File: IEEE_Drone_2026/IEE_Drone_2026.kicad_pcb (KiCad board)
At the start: 2 copper layers, 40.5 x 58 mm, 30 parts, among them IC1 TPSM84209RKHT, IC2 TPSM84209RKHT, J1 ESC, J10 M2, J11 Conn_01x02_Socket, J2 M4 Mounting, J3 M4 Mounting, J4 M4 Mounting, J5 M4 Mounting, J6 Pixy2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

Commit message: made production
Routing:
- net GND: vias 25 -> 27
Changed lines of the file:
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@@
+	)
+	(via
+		(at 99.06 65.532)
+		(size 0.6)
+		(drill 0.3)
+		(layers "F.Cu" "B.Cu")
+		(free yes)
+		(net 29)
+	)
+	(via
+		(at 99.06 64.643)
+		(size 0.6)
+		(drill 0.3)
+		(layers "F.Cu" "B.Cu")
+		(free yes)
+		(net 29)
 	)
 	(via

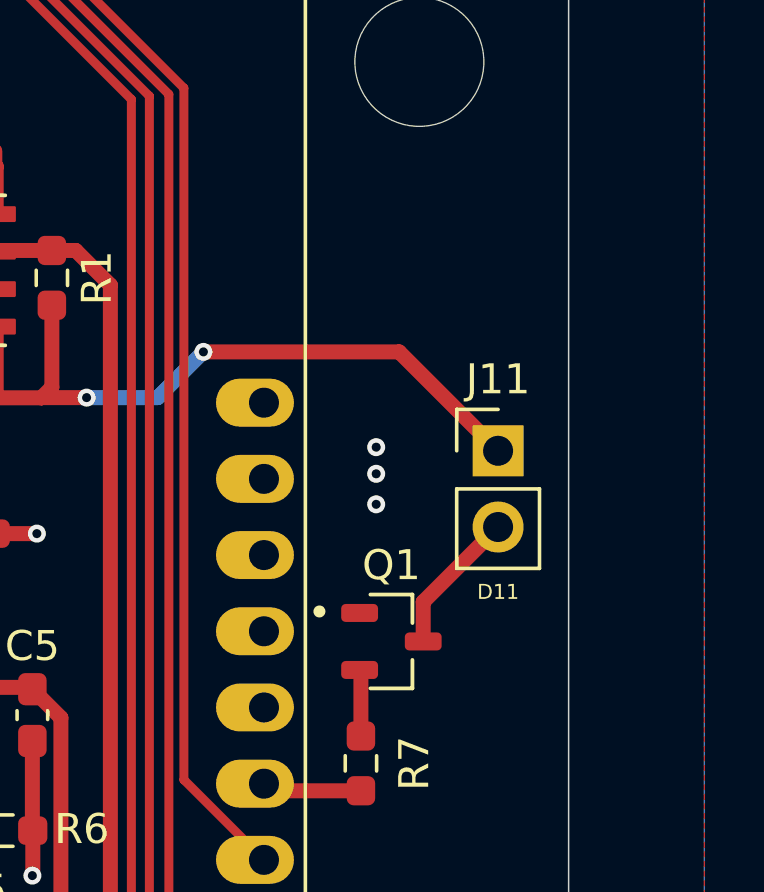
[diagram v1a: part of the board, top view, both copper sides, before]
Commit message: updated silkscreen text
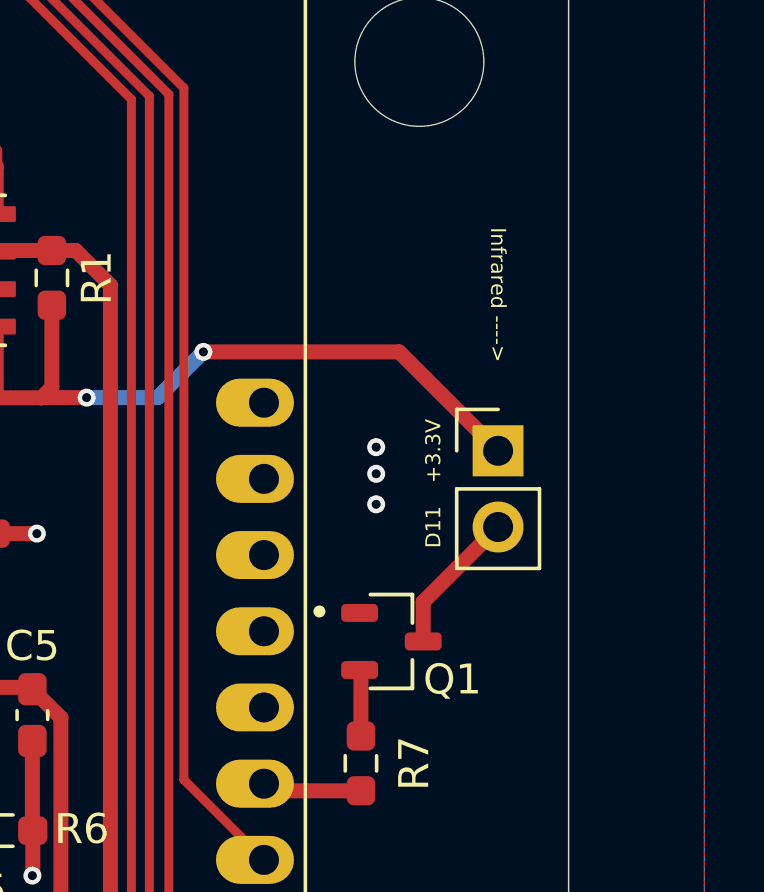
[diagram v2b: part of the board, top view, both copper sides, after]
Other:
- board text added: "Infrared ---->"
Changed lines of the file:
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@@
 			(at 0 -2.38 0)
 			(layer "F.SilkS")
+			(hide yes)
 			(effects
 				(font
@@
 		(at 99.568 71.12)
 		(property "Reference" "Q1"
-			(at 0 -2.54 0)
+			(at 2.032 1.27 0)
 			(layer "F.SilkS")
 			(effects
@@
 		)
 	)
+	(gr_text "Infrared ---->\n"
+		(at 103.124 59.563 270)
+		(layer "F.SilkS")
+		(effects
+			(font
+				(size 0.5 0.5)
+				(thickness 0.125)
+			)
+		)
+	)
 	(gr_text "SCK"
 		(at 69.6 63.8 90)
@@
 		)
 	)
+	(gr_text "+3.3V"
+		(at 100.965 64.77 90)
+		(layer "F.SilkS")
+		(effects
+			(font
+				(size 0.5 0.5)
+				(thickness 0.125)
+			)
+		)
+	)
 	(gr_text "D9\n"
 		(at 86 43.9 0)
@@
 	)
 	(gr_text "D11\n"
-		(at 103.124 69.469 0)
+		(at 100.965 67.31 90)
 		(layer "F.SilkS")
 		(effects

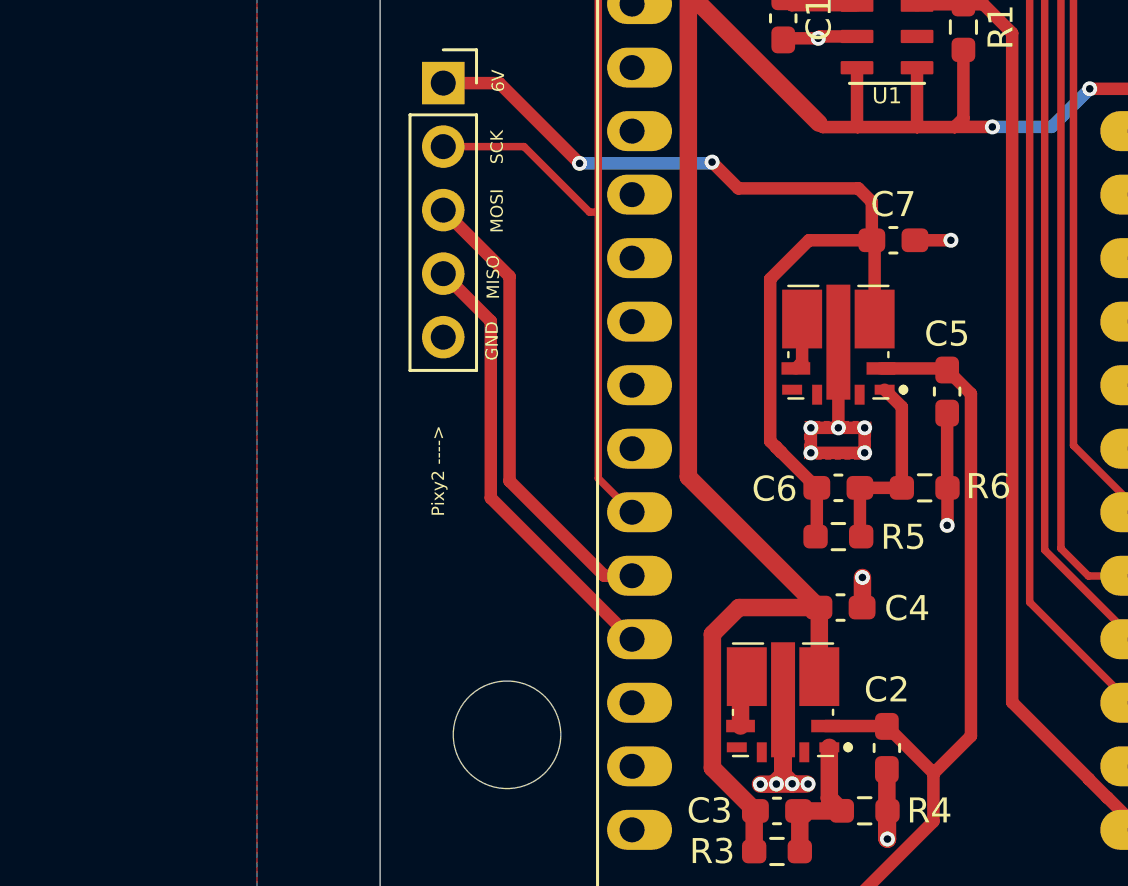
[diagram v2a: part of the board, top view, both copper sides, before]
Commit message: updated c4 c5 c7 to 1206
coudn't find 0603 in spec
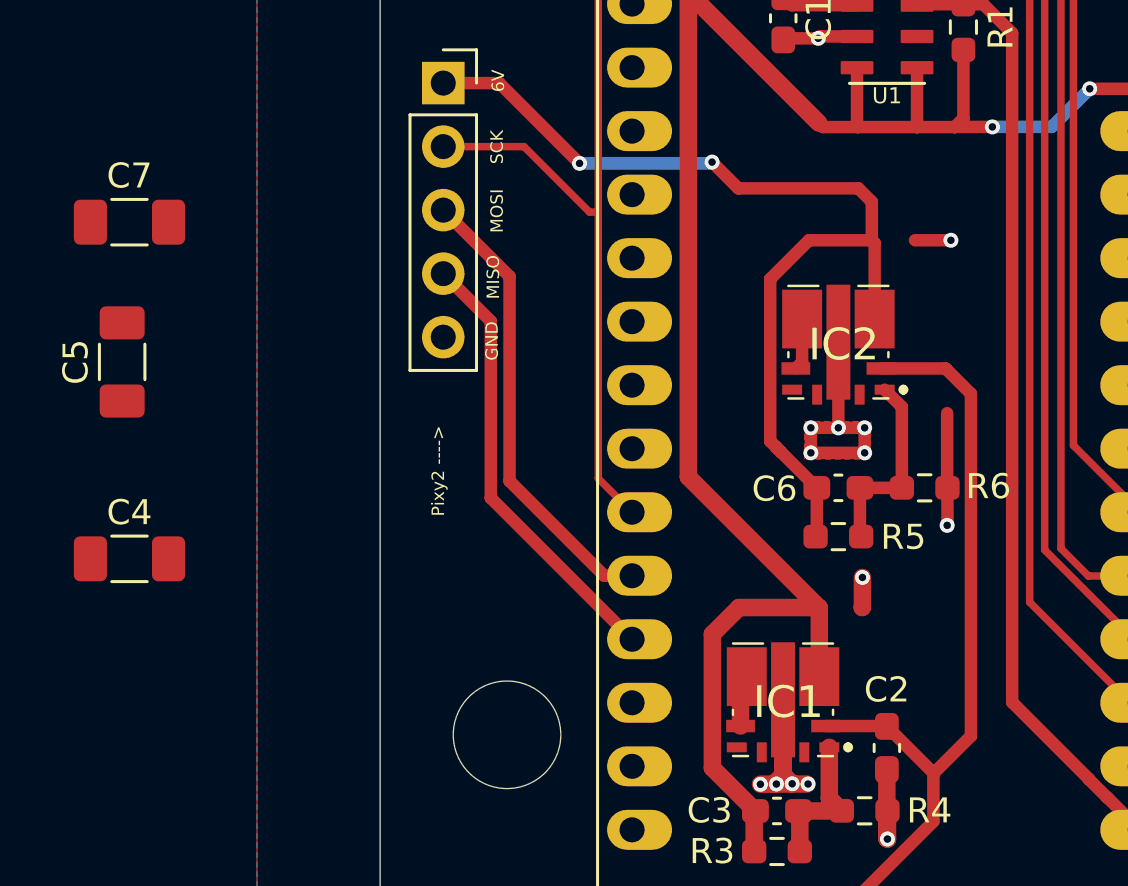
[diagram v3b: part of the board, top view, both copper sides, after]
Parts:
- C4, C5, C7: footprint Capacitor_SMD:C_0603_1608Metric_Pad1.08x0.95mm_HandSolder -> Capacitor_SMD:C_1206_3216Metric_Pad1.33x1.80mm_HandSolder
- R3, R5: value 10kOhm -> 10k
- R4: value 2.2kOhm -> 2.2k
- moved C5 33.0 mm to (54.6, 72.4)
- moved C7 30.6 mm to (54.9, 66.8)
- moved C4 28.5 mm to (54.9, 80.3)

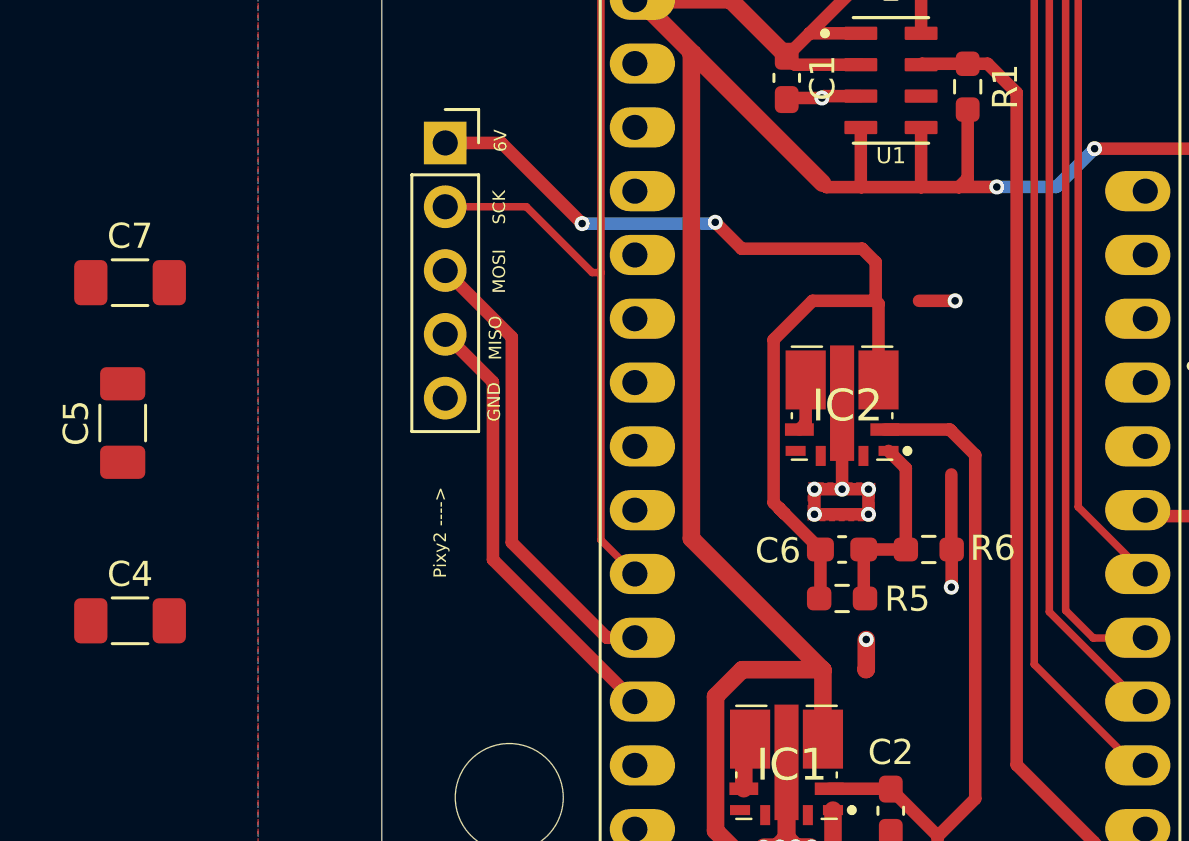
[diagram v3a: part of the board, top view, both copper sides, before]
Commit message: updated routing for 1206 caps
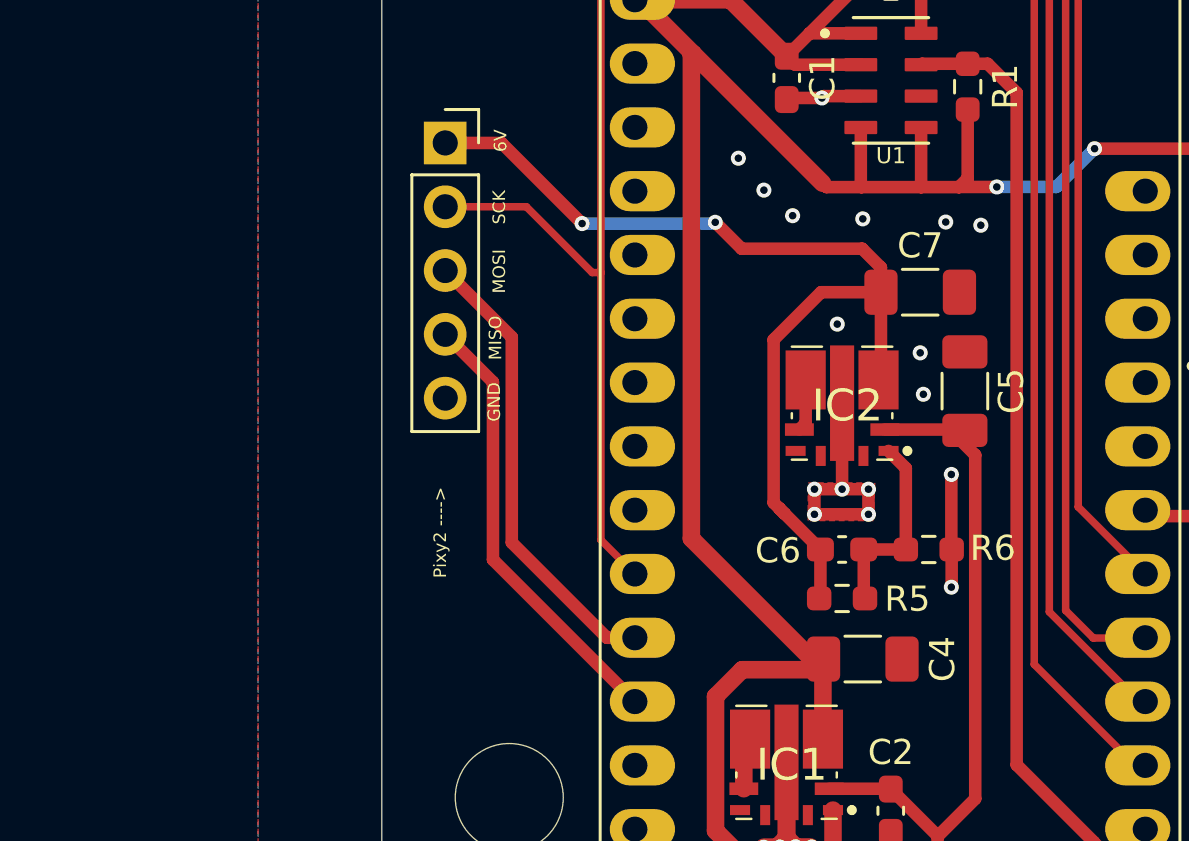
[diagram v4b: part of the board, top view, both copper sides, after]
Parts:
- moved C5 33.6 mm to (88.1, 71.1), turned to -90 degrees
- moved C7 31.5 mm to (86.4, 67.2)
- moved C4 29.2 mm to (84.1, 81.8)
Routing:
- net GND: track 33.4 -> 30.7 mm, vias 27 -> 35
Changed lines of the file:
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@@
 	(footprint "Capacitor_SMD:C_1206_3216Metric_Pad1.33x1.80mm_HandSolder"
 		(layer "F.Cu")
-		(at 54.9025 80.264)
+		(at 84.074 81.788)
 		(descr "Capacitor SMD 1206 (3216 Metric), square (rectangular) end terminal, IPC-7351 nominal with elongated pad for handsoldering. (Body size source: IPC-SM-782 page 76, https://www.pcb-3d.com/wordpress/wp-content/uploads/ipc-sm-782a_amendment_1_and_2.pdf), generated with kicad-footprint-generator")
 		(tags "capacitor handsolder")
 		(property "Reference" "C4"
-			(at 0 -1.85 0)
+			(at 3.175 0 90)
 			(layer "F.SilkS")
 			(effects
@@
 			(at 0 1.85 0)
 			(layer "F.Fab")
+			(hide yes)
 			(effects
 				(font
@@
 	(footprint "Capacitor_SMD:C_1206_3216Metric_Pad1.33x1.80mm_HandSolder"
 		(layer "F.Cu")
-		(at 54.61 72.39 90)
+		(at 88.138 71.12 -90)
 		(descr "Capacitor SMD 1206 (3216 Metric), square (rectangular) end terminal, IPC-7351 nominal with elongated pad for handsoldering. (Body size source: IPC-SM-782 page 76, https://www.pcb-3d.com/wordpress/wp-content/uploads/ipc-sm-782a_amendment_1_and_2.pdf), generated with kicad-footprint-generator")
 		(tags "capacitor handsolder")
@@
 			(at 0 1.85 90)
 			(layer "F.Fab")
+			(hide yes)
 			(effects
 				(font
@@
 		(attr smd)
 		(fp_line
-			(start -0.711252 -0.91)
-			(end 0.711252 -0.91)
+			(start -0.711252 0.91)
+			(end 0.711252 0.91)
 			(stroke
 				(width 0.12)
@@
 		)
 		(fp_line
-			(start -0.711252 0.91)
-			(end 0.711252 0.91)
+			(start -0.711252 -0.91)
+			(end 0.711252 -0.91)
 			(stroke
 				(width 0.12)
@@
 		)
 		(fp_line
-			(start 2.48 -1.15)
-			(end 2.48 1.15)
+			(start -2.48 1.15)
+			(end -2.48 -1.15)
 			(stroke
 				(width 0.05)
@@
 		)
 		(fp_line
-			(start -2.48 -1.15)
-			(end 2.48 -1.15)
+			(start 2.48 1.15)
+			(end -2.48 1.15)
 			(stroke
 				(width 0.05)
@@
 		)
 		(fp_line
-			(start 2.48 1.15)
-			(end -2.48 1.15)
+			(start -2.48 -1.15)
+			(end 2.48 -1.15)
 			(stroke
 				(width 0.05)
@@
 		)
 		(fp_line
-			(start -2.48 1.15)
-			(end -2.48 -1.15)
+			(start 2.48 -1.15)
+			(end 2.48 1.15)
 			(stroke
 				(width 0.05)
@@
 		)
 		(fp_line
-			(start 1.6 -0.8)
-			(end 1.6 0.8)
+			(start -1.6 0.8)
+			(end -1.6 -0.8)
 			(stroke
 				(width 0.1)
@@
 		)
 		(fp_line
-			(start -1.6 -0.8)
-			(end 1.6 -0.8)
+			(start 1.6 0.8)
+			(end -1.6 0.8)
 			(stroke
 				(width 0.1)
@@
 		)
 		(fp_line
-			(start 1.6 0.8)
-			(end -1.6 0.8)
+			(start -1.6 -0.8)
+			(end 1.6 -0.8)
 			(stroke
 				(width 0.1)
@@
 		)
 		(fp_line
-			(start -1.6 0.8)
-			(end -1.6 -0.8)
+			(start 1.6 -0.8)
+			(end 1.6 0.8)
 			(stroke
 				(width 0.1)
@@
 		)
 		(pad "1" smd roundrect
-			(at -1.5625 0 90)
+			(at -1.5625 0 270)
 			(size 1.325 1.8)
 			(layers "F.Cu" "F.Mask" "F.Paste")
@@
 		)
 		(pad "2" smd roundrect
-			(at 1.5625 0 90)
+			(at 1.5625 0 270)
 			(size 1.325 1.8)
 			(layers "F.Cu" "F.Mask" "F.Paste")
@@
 	(footprint "Capacitor_SMD:C_1206_3216Metric_Pad1.33x1.80mm_HandSolder"
 		(layer "F.Cu")
-		(at 54.9025 66.802)
+		(at 86.36 67.183)
 		(descr "Capacitor SMD 1206 (3216 Metric), square (rectangular) end terminal, IPC-7351 nominal with elongated pad for handsoldering. (Body size source: IPC-SM-782 page 76, https://www.pcb-3d.com/wordpress/wp-content/uploads/ipc-sm-782a_amendment_1_and_2.pdf), generated with kicad-footprint-generator")
 		(tags "capacitor handsolder")
@@
 			(at 0 1.85 0)
 			(layer "F.Fab")
+			(hide yes)
 			(effects
 				(font
@@
 	)
 	(segment
-		(start 86.3125 67.525)
-		(end 87.75 67.525)
-		(width 0.5)
-		(layer "F.Cu")
-		(net 29)
-	)
-	(segment
 		(start 82.15 75.025)
 		(end 83.25 75.025)
@@
 	)
 	(segment
-		(start 84.2122 81.0086)
-		(end 84.2122 82.1976)
-		(width 0.7)
-		(layer "F.Cu")
-		(net 29)
-	)
-	(segment
 		(start 85.213 90.34)
 		(end 85.213 90.7394)
@@
 	)
 	(segment
-		(start 84.2122 82.1976)
-		(end 84.1978 82.212)
-		(width 0.7)
-		(layer "F.Cu")
-		(net 29)
-	)
-	(segment
 		(start 80.7722 89.2686)
 		(end 81.9865 89.2686)
@@
 	)
 	(via
+		(at 87.376 64.389)
+		(size 0.6)
+		(drill 0.3)
+		(layers "F.Cu" "B.Cu")
+		(free yes)
+		(net 29)
+	)
+	(via
 		(at 81.4022 89.2586)
 		(size 0.6)
@@
 	)
 	(via
+		(at 79.121 61.849)
+		(size 0.6)
+		(drill 0.3)
+		(layers "F.Cu" "B.Cu")
+		(free yes)
+		(net 29)
+	)
+	(via
 		(at 84.3 75.025)
 		(size 0.6)
@@
 	)
 	(via
+		(at 80.137 63.119)
+		(size 0.6)
+		(drill 0.3)
+		(layers "F.Cu" "B.Cu")
+		(free yes)
+		(net 29)
+	)
+	(via
+		(at 86.36 69.596)
+		(size 0.6)
+		(drill 0.3)
+		(layers "F.Cu" "B.Cu")
+		(free yes)
+		(net 29)
+	)
+	(via
 		(at 90.25 98.25)
 		(size 0.6)
@@
 	)
 	(via
-		(at 84.2122 81.0086)
+		(at 84.074 64.262)
 		(size 0.6)
 		(drill 0.3)
@@
 	)
 	(via
+		(at 88.773 64.516)
+		(size 0.6)
+		(drill 0.3)
+		(layers "F.Cu" "B.Cu")
+		(free yes)
+		(net 29)
+	)
+	(via
+		(at 81.28 64.135)
+		(size 0.6)
+		(drill 0.3)
+		(layers "F.Cu" "B.Cu")
+		(free yes)
+		(net 29)
+	)
+	(via
+		(at 87.6 74.4375)
+		(size 0.6)
+		(drill 0.3)
+		(layers "F.Cu" "B.Cu")
+		(net 29)
+	)
+	(via
 		(at 99.06 65.532)
 		(size 0.6)
@@
 	)
 	(via
-		(at 99.06 64.643)
+		(at 83.058 68.453)
 		(size 0.6)
 		(drill 0.3)
@@
 	)
 	(via
-		(at 82.15 76.025)
+		(at 99.06 64.643)
 		(size 0.6)
 		(drill 0.3)
@@
 	)
 	(via
-		(at 87.75 67.525)
+		(at 82.15 76.025)
 		(size 0.6)
 		(drill 0.3)
 		(layers "F.Cu" "B.Cu")
+		(free yes)
 		(net 29)
 	)
@@
 	)
 	(via
+		(at 86.487 71.247)
+		(size 0.6)
+		(drill 0.3)
+		(layers "F.Cu" "B.Cu")
+		(free yes)
+		(net 29)
+	)
+	(via
 		(at 95.75 98.25)
 		(size 0.6)
@@
 	)
 	(segment
-		(start 82.3875 79.325)
-		(end 82.3375 79.375)
+		(start 84.7975 67.183)
+		(end 84.7975 70.5775)
 		(width 0.5)
 		(layer "F.Cu")
@@
 	)
 	(segment
-		(start 69.69 61.24)
-		(end 67.45 61.24)
+		(start 82.3875 79.325)
+		(end 82.3375 79.375)
 		(width 0.5)
 		(layer "F.Cu")
@@
 	)
 	(segment
-		(start 84.05 65.45)
-		(end 79.25 65.45)
+		(start 84.7975 66.1975)
+		(end 84.7975 67.183)
 		(width 0.5)
 		(layer "F.Cu")
@@
 	)
 	(segment
-		(start 72.9 64.45)
-		(end 69.69 61.24)
+		(start 80.96875 76.00625)
+		(end 80.524 75.5615)
 		(width 0.5)
 		(layer "F.Cu")
@@
 	)
 	(segment
-		(start 82.3875 77.425)
-		(end 80.96875 76.00625)
+		(start 69.69 61.24)
+		(end 67.45 61.24)
 		(width 0.5)
 		(layer "F.Cu")
@@
 	)
 	(segment
-		(start 82.3875 77.425)
-		(end 82.3875 79.325)
+		(start 84.05 65.45)
+		(end 79.25 65.45)
 		(width 0.5)
 		(layer "F.Cu")
@@
 	)
 	(segment
-		(start 84.5875 65.9875)
-		(end 84.5875 67.525)
+		(start 84.05 65.45)
+		(end 84.7975 66.1975)
 		(width 0.5)
 		(layer "F.Cu")
@@
 	)
 	(segment
-		(start 79.25 65.45)
-		(end 78.2 64.4)
+		(start 72.9 64.45)
+		(end 69.69 61.24)
 		(width 0.5)
 		(layer "F.Cu")
@@
 	)
 	(segment
-		(start 82.073 67.525)
-		(end 80.524 69.074)
+		(start 84.7975 70.5775)
+		(end 84.7 70.675)
 		(width 0.5)
 		(layer "F.Cu")
@@
 	)
 	(segment
-		(start 84.05 65.45)
-		(end 84.5875 65.9875)
+		(start 82.3875 77.425)
+		(end 80.96875 76.00625)
 		(width 0.5)
 		(layer "F.Cu")
@@
 	)
 	(segment
-		(start 84.5875 67.525)
-		(end 82.073 67.525)
+		(start 82.3875 77.425)
+		(end 82.3875 79.325)
 		(width 0.5)
 		(layer "F.Cu")
@@
 	)
 	(segment
-		(start 80.96875 76.00625)
-		(end 80.75 75.7875)
+		(start 79.25 65.45)
+		(end 78.2 64.4)
 		(width 0.5)
 		(layer "F.Cu")
@@
 	(segment
 		(start 80.524 75.5615)
-		(end 80.96875 76.00625)
+		(end 80.524 69.074)
 		(width 0.5)
 		(layer "F.Cu")
@@
 	)
 	(segment
-		(start 84.7 67.6375)
-		(end 84.5875 67.525)
+		(start 82.415 67.183)
+		(end 84.7975 67.183)
 		(width 0.5)
 		(layer "F.Cu")
@@
 	)
 	(segment
-		(start 80.524 69.074)
-		(end 80.524 75.5615)
+		(start 80.96875 76.00625)
+		(end 80.75 75.7875)
 		(width 0.5)
 		(layer "F.Cu")
@@
 	)
 	(segment
-		(start 84.7 70.675)
-		(end 84.7 67.6375)
+		(start 80.524 69.074)
+		(end 82.415 67.183)
 		(width 0.5)
 		(layer "F.Cu")

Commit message: cleaned up routing and merlin image
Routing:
- net GND: vias 35 -> 32
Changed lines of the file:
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@@
-	)
-	(via
-		(at 86.36 69.596)
-		(size 0.6)
-		(drill 0.3)
-		(layers "F.Cu" "B.Cu")
-		(free yes)
-		(net 29)
 	)
 	(via
@@
 	)
 	(via
-		(at 84.074 64.262)
-		(size 0.6)
-		(drill 0.3)
-		(layers "F.Cu" "B.Cu")
-		(free yes)
-		(net 29)
-	)
-	(via
 		(at 83.25 75.025)
 		(size 0.6)
@@
 	(via
 		(at 99.06 65.532)
-		(size 0.6)
-		(drill 0.3)
-		(layers "F.Cu" "B.Cu")
-		(free yes)
-		(net 29)
-	)
-	(via
-		(at 83.058 68.453)
 		(size 0.6)
 		(drill 0.3)
@@
 			)
 		)
+	)
+	(zone
+		(net 0)
+		(net_name "")
+		(layer "F.Cu")
+		(hatch edge 0.5)
+		(connect_pads
+			(clearance 0)
+		)
+		(min_thickness 0.25)
+		(filled_areas_thickness no)
+		(keepout
+			(tracks not_allowed)
+			(vias not_allowed)
+			(pads not_allowed)
+			(copperpour not_allowed)
+			(footprints allowed)
+		)
+		(placement
+			(enabled no)
+			(sheetname "/")
+		)
+		(fill
+			(thermal_gap 0.5)
+			(thermal_bridge_width 0.5)
+		)
+		(polygon
+			(pts
+				(xy 81.661 67.691) (xy 84.328 67.818) (xy 84.201 69.342) (xy 82.677 69.469) (xy 81.534 69.342)
+			)
+		)
